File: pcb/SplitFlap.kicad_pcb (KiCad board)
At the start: 2 copper layers, 35 x 35 mm, 17 parts, among them U1 PCF8575DBR, U2 ULN2003

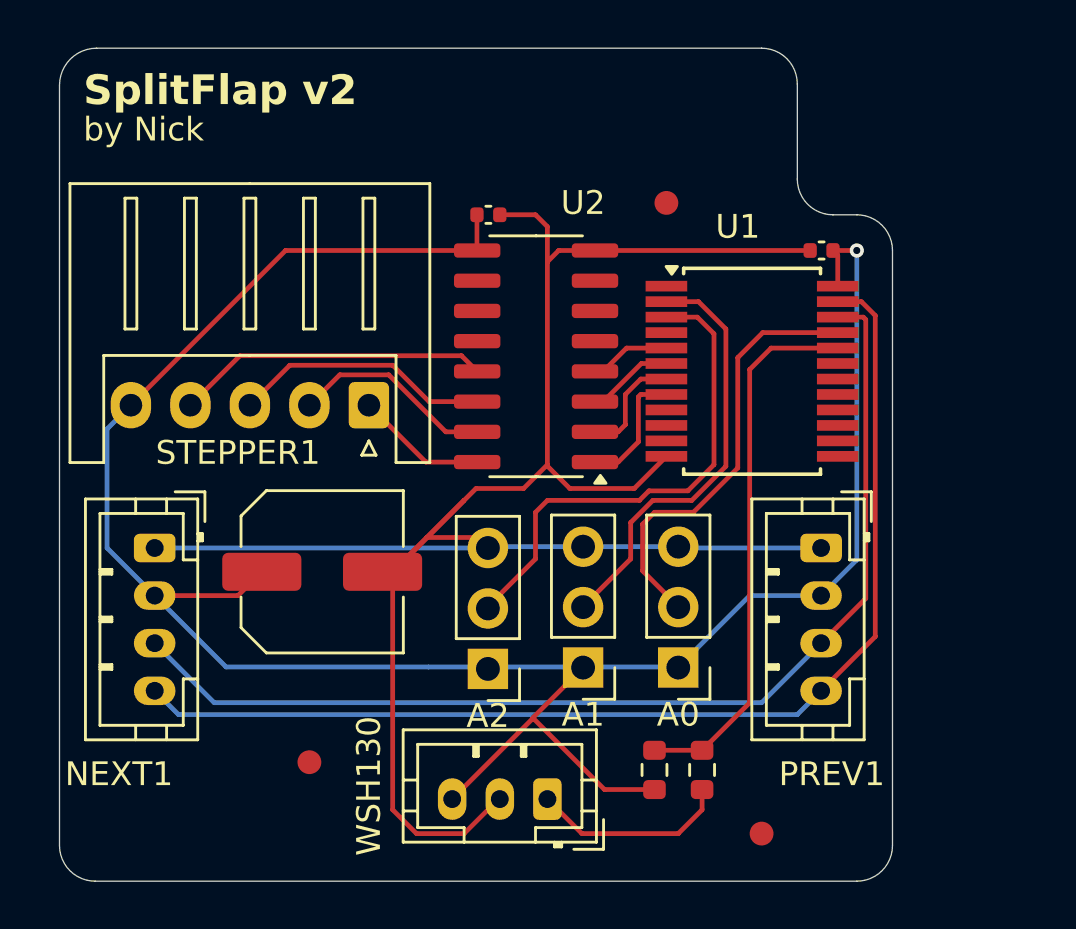
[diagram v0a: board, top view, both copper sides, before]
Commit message: Accomodate linear regulator and new address pins on PCB
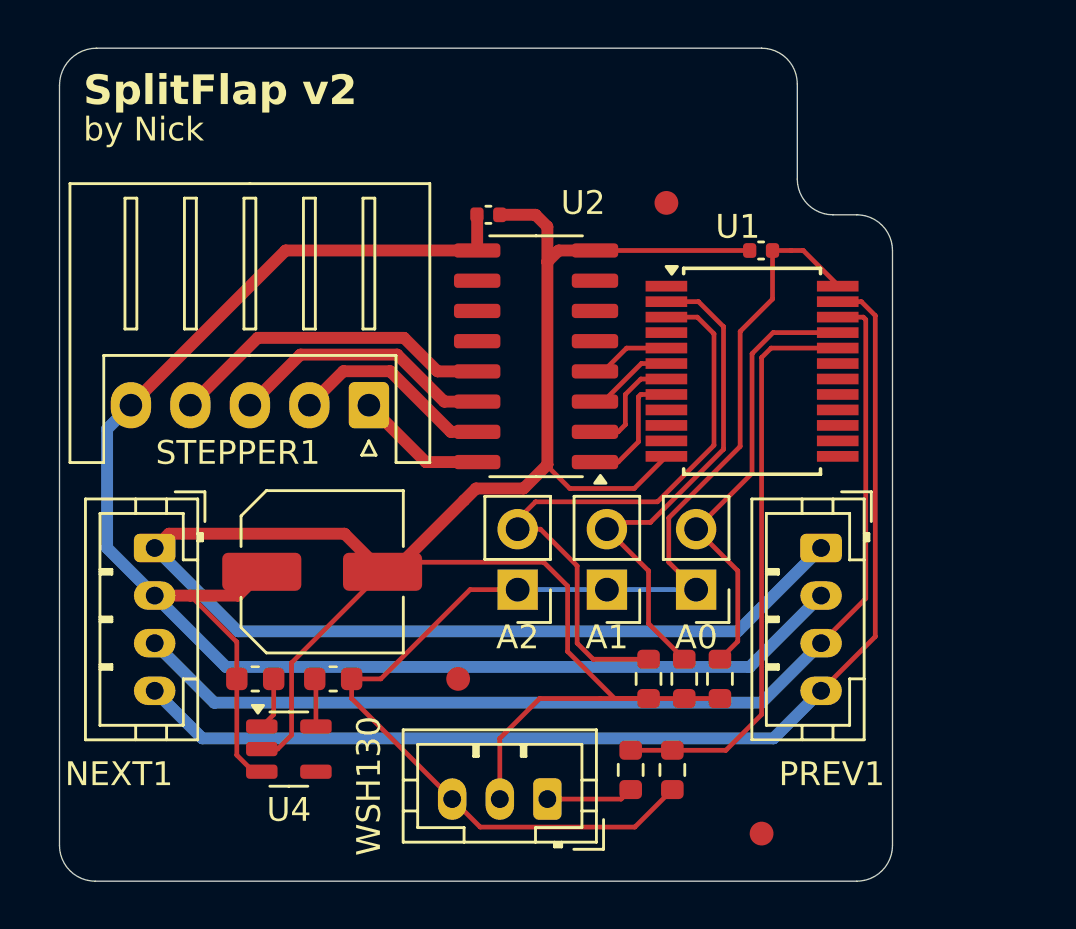
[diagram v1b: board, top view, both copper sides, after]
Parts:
- added C2: 1 µF, Capacitor_SMD:C_0603_1608Metric, F.Cu at (153.2, 86.0)
- added C3: 1 µF, Capacitor_SMD:C_0603_1608Metric, F.Cu at (156.5, 86.0)
- added PULL_UP3: 10K, Resistor_SMD:R_0603_1608Metric, F.Cu at (172.8, 86.0)
- added PULL_UP4: 10K, Resistor_SMD:R_0603_1608Metric, F.Cu at (171.2, 86.0)
- added PULL_UP5: 10K, Resistor_SMD:R_0603_1608Metric, F.Cu at (169.8, 86.0)
- added U4: AP2112K-3.3, Package_TO_SOT_SMD:SOT-23-5, F.Cu at (154.6, 89.0)
- A0, A1, A2: value Conn_01x03_Pin -> Conn_01x02_Pin; footprint Connector_PinHeader_2.54mm:PinHeader_1x03_P2.54mm_Vertical -> Connector_PinHeader_2.54mm:PinHeader_1x02_P2.54mm_Vertical
- moved REF** 7.16 mm to (161.8, 86.0)
- moved A2 3.56 mm to (164.2, 82.2)
- moved A1 3.42 mm to (168.0, 82.2)
- moved A0 3.36 mm to (171.8, 82.2)
- moved SERIES1 3.00 mm to (169.0, 89.8)
- moved C1 2.54 mm to (174.5, 68.0)
- moved PULL_UP2 0.75 mm to (170.8, 89.8)
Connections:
- A0 pad 1: +5V -> +3.3V
- A1 pad 1: +5V -> +3.3V
- A2 pad 1: +5V -> +3.3V
- C1 pad 1: +5V -> +3.3V
- C3_BULK1 pad 1: +5V -> GND
- C3_BULK1 pad 2: GND -> +5V
- PULL_UP2 pad 1: +5V -> +3.3V
- U1 pad 24: +5V -> +3.3V
- WSH130 pad 3: +5V -> +3.3V
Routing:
- net +3.3V: track 0.00 -> 53.5 mm
- net GND: track 89.5 -> 115.5 mm
- net +5V: track 95.5 -> 71.9 mm, vias 1 -> 0
- net Net-(A2-Pin_2): track 20.9 -> 26.2 mm
- net Net-(WSH130-Pin_1): track 8.36 -> 3.67 mm
- net Net-(A1-Pin_2): track 18.1 -> 20.7 mm
- net Net-(U4-VIN): track 0.00 -> 2.21 mm
- net Net-(U4-VOUT): track 0.00 -> 2.02 mm
- net Net-(U1-P17): track 22.9 -> 24.5 mm
- net Net-(NEXT1-Pin_4): track 47.4 -> 48.2 mm
- net Net-(STEPPER1-Pin_4): track 13.2 -> 13.8 mm

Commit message: Minor pcb changes
- Updates the position of the entire board down,
- Adds an edge cut section for the WSH130 wiring.
- Moves the ULN2003 up a bit to clean up the connections.
- Updates silkscreen labels.
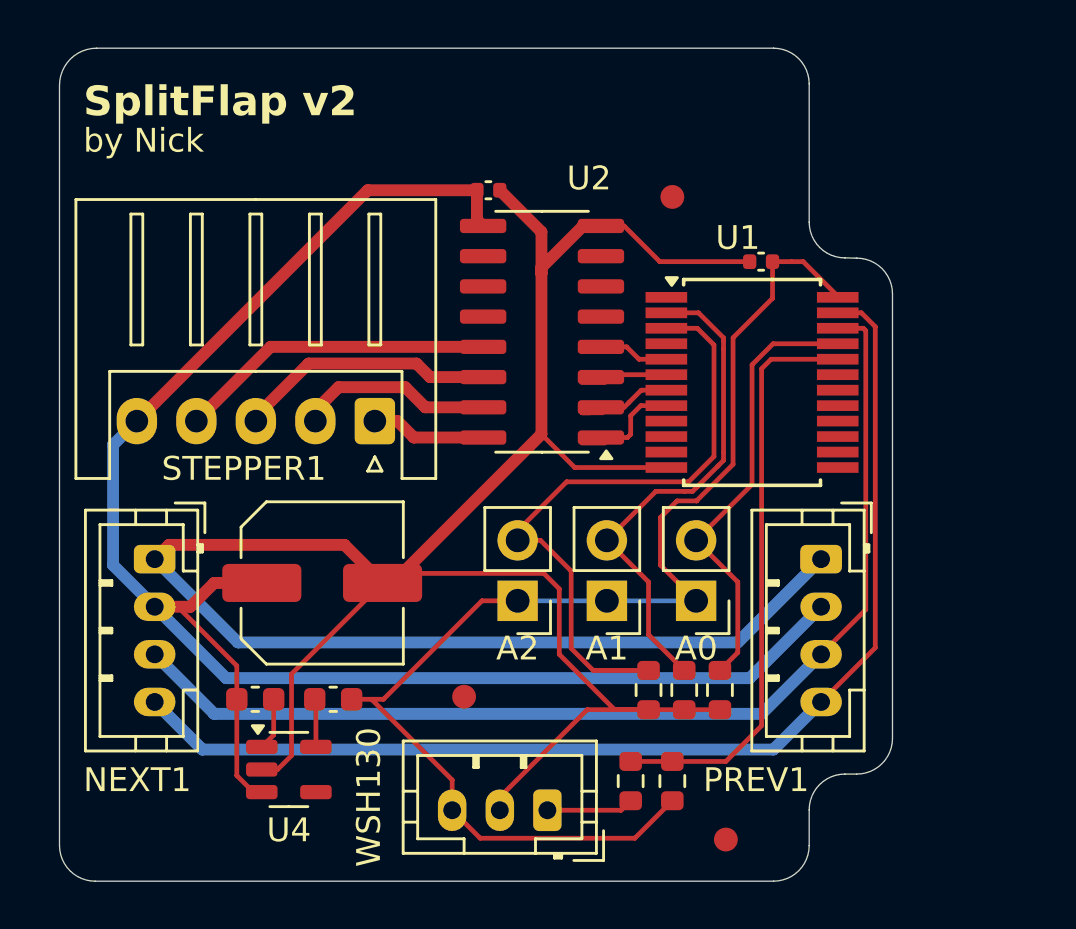
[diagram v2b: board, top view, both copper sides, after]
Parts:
- moved REF** 1.52 mm to (173.0, 92.8)
- moved U2 1.06 mm to (165.3, 71.4)
- moved C2_BYPASS1 1.03 mm to (163.0, 65.5)
- moved C2 0.86 mm to (153.2, 86.9)
- moved C3 0.86 mm to (156.5, 86.9)
- moved U4 0.86 mm to (154.6, 89.8)
- moved REF** 0.79 mm to (162.0, 86.8)
- moved STEPPER1 0.71 mm to (158.2, 75.2)
- moved WSH130 0.47 mm to (165.5, 91.5)
- moved A0 0.47 mm to (171.8, 82.7)
- moved A1 0.47 mm to (168.0, 82.7)
- moved A2 0.47 mm to (164.2, 82.7)
- moved C1 0.47 mm to (174.5, 68.5)
- moved C3_BULK1 0.47 mm to (156.0, 82.0)
- moved NEXT1 0.47 mm to (149.0, 81.0)
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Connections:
- C3_BULK1 pad 1: GND -> +5V
- C3_BULK1 pad 2: +5V -> GND
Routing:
- net +5V: track 71.9 -> 74.7 mm
- net Net-(U1-P4): track 6.44 -> 4.73 mm
- net Net-(U1-P1): track 4.38 -> 2.97 mm
- net Net-(U1-P3): track 5.64 -> 4.27 mm
- net Net-(U1-P2): track 4.88 -> 3.76 mm
- net Net-(STEPPER1-Pin_1): track 5.54 -> 4.84 mm
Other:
- outline, holes or cut-outs redrawn
- board text added: "+3.3V"

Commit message: Rewire PCB
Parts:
- removed A0, A1, A2: Conn_01x02_Pin, Connector_PinHeader_2.54mm:PinHeader_1x02_P2.54mm_Vertical
- added J1: A1_3, Connector_PinHeader_2.54mm:PinHeader_2x03_P2.54mm_Vertical, F.Cu at (177.0, 74.0)
- added PULL_UP6: 4K7, Resistor_SMD:R_0603_1608Metric, F.Cu at (162.8, 85.5)
- added PULL_UP7: 4k7, Resistor_SMD:R_0603_1608Metric, F.Cu at (162.8, 84.0)
- added PULL_UP8: 4k7, Resistor_SMD:R_0603_1608Metric, F.Cu at (162.8, 82.5)
- added PULL_UP9: 4k7, Resistor_SMD:R_0603_1608Metric, F.Cu at (162.8, 81.0)
- moved REF** 23.3 mm to (149.8, 91.8)
- moved C1 20.2 mm to (172.2, 88.5)
- moved PULL_UP5 17.9 mm to (174.0, 69.1), turned to 90 degrees
- moved PULL_UP3 17.5 mm to (171.0, 69.1), turned to 90 degrees
- moved PULL_UP4 17.4 mm to (172.5, 69.1), turned to 90 degrees
- moved REF** 13.1 mm to (174.0, 92.0)
- moved U1 10.8 mm to (169.1, 83.1), turned to -90 degrees
- moved REF** 4.78 mm to (174.0, 62.2)
- moved PULL_UP2 1.60 mm to (169.2, 89.8)
- moved C2_BYPASS1 1.55 mm to (162.4, 66.9)
- moved SERIES1 1.36 mm to (167.8, 89.8)
- moved WSH130 1.27 mm to (164.2, 91.3)
- moved U2 1.24 mm to (165.2, 72.7)
- moved C3 0.60 mm to (155.9, 87.1)
- moved C2 0.33 mm to (153.0, 87.1), turned to 180 degrees
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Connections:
- C2 pad 1: +5V -> GND
- C2 pad 2: Net-(U4-VIN) -> +5V
- C3 pad 1: Net-(U4-VOUT) -> GND
- PULL_UP3 pad 1: Net-(A0-Pin_2) -> Net-(J1-Pin_6)
- PULL_UP5 pad 1: Net-(A2-Pin_2) -> Net-(J1-Pin_2)
- U1 pad 21: Net-(A0-Pin_2) -> Net-(J1-Pin_2)
- U1 pad 3: Net-(A2-Pin_2) -> Net-(J1-Pin_6)
- U4 pad 1: Net-(U4-VIN) -> +5V
- U4 pad 5: Net-(U4-VOUT) -> +3.3V
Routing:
- net Net-(A2-Pin_2): track 26.2 -> 0.00 mm
- net Net-(J1-Pin_2): track 0.00 -> 21.0 mm
- net Net-(U1-P17): track 24.5 -> 4.06 mm
- net Net-(A0-Pin_2): track 18.5 -> 0.00 mm
- net Net-(U1-P1): track 2.97 -> 17.3 mm
- net Net-(NEXT1-Pin_4): track 48.2 -> 34.7 mm
- net Net-(U1-P2): track 3.76 -> 15.5 mm
- net Net-(NEXT1-Pin_3): track 45.7 -> 35.0 mm
- net Net-(J1-Pin_6): track 0.00 -> 10.4 mm
- net Net-(J1-Pin_4): track 20.7 -> 11.8 mm
- net Net-(U1-P3): track 4.27 -> 13.2 mm
- net +3.3V: track 53.7 -> 62.5 mm
- net GND: track 116.0 -> 120.6 mm
- net Net-(U1-P4): track 4.73 -> 9.33 mm
- net +5V: track 74.7 -> 71.5 mm
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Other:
- board text added: "A1"
- board text added: "A2"
- board text added: "A3"
- board text added: "SplitFlap v3"
- board text removed: "SplitFlap v2"

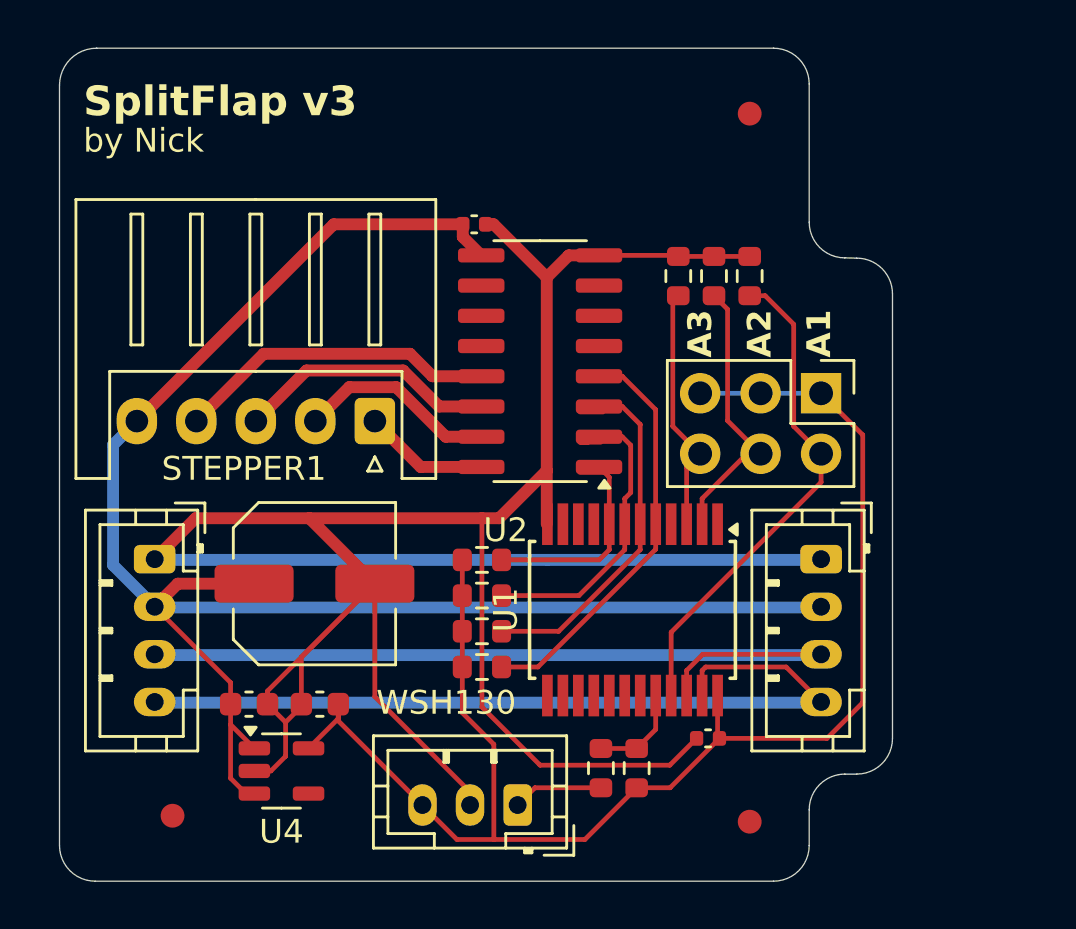
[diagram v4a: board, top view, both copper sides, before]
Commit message: Eliminate 3.3v line from PCB
Based on the findings by FoxManJ the 3.3v line is not required if we
use a 4.7k Ohm pull-up to 5v for the SCL and SDA lines coming from the
ESP32.

By using this pull-up to 5V we eliminate the need for the PCF8575 to
run at 3.3v to understand the signals from the ESP32, which was the
reason I originally implemented the 3.3v line on each board.
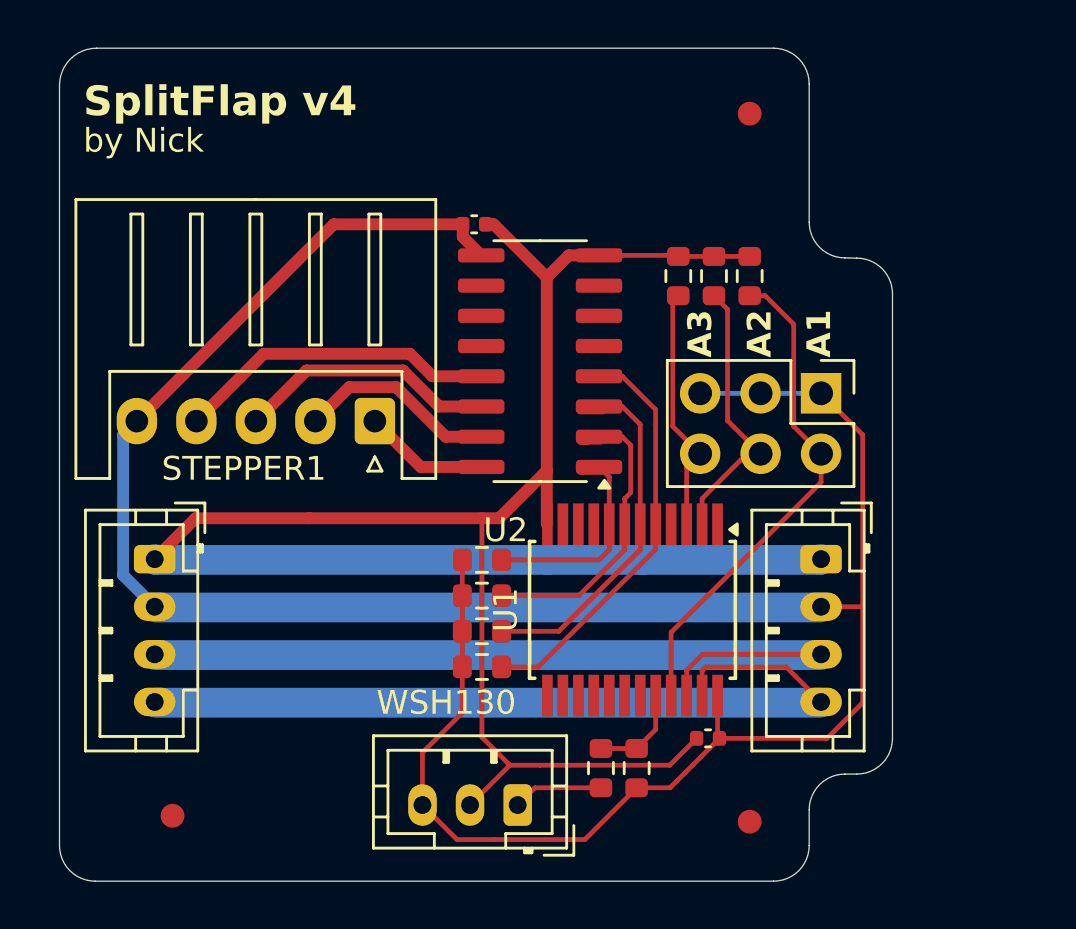
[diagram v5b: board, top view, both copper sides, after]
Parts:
- removed C2, C3: 1 µF, Capacitor_SMD:C_0603_1608Metric
- removed C3_BULK1: 220 µF, Capacitor_SMD:C_Elec_6.3x7.7
- removed U4: AP2112K-3.3, Package_TO_SOT_SMD:SOT-23-5
- PULL_DOWN3: renamed from PULL_UP3; value 10K -> 47K
- PULL_DOWN4: renamed from PULL_UP4; value 10K -> 47K
- PULL_DOWN5: renamed from PULL_UP5; value 10K -> 47K
- PULL_UP6: value 4K7 -> 2k2
- PULL_UP7, PULL_UP8, PULL_UP9: value 4k7 -> 2k2
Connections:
- C1 pad 1: +3.3V -> +5V
- J1 pad 1: +3.3V -> +5V
- J1 pad 3: +3.3V -> +5V
- J1 pad 5: +3.3V -> +5V
- PULL_UP2 pad 1: +3.3V -> +5V
- PULL_UP6 pad 1: +3.3V -> +5V
- PULL_UP7 pad 1: +3.3V -> +5V
- PULL_UP8 pad 1: +3.3V -> +5V
- PULL_UP9 pad 1: +3.3V -> +5V
- U1 pad 24: +3.3V -> +5V
- WSH130 pad 3: +3.3V -> +5V
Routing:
- net +3.3V: track 62.5 -> 0.00 mm
- net +5V: track 71.5 -> 110.2 mm
- net GND: track 120.6 -> 91.0 mm
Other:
- board text added: "SplitFlap v4"
- board text removed: "SplitFlap v3"

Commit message: Use pinsocket and headers for board to board connector
Eliminates the JST cables between boards.
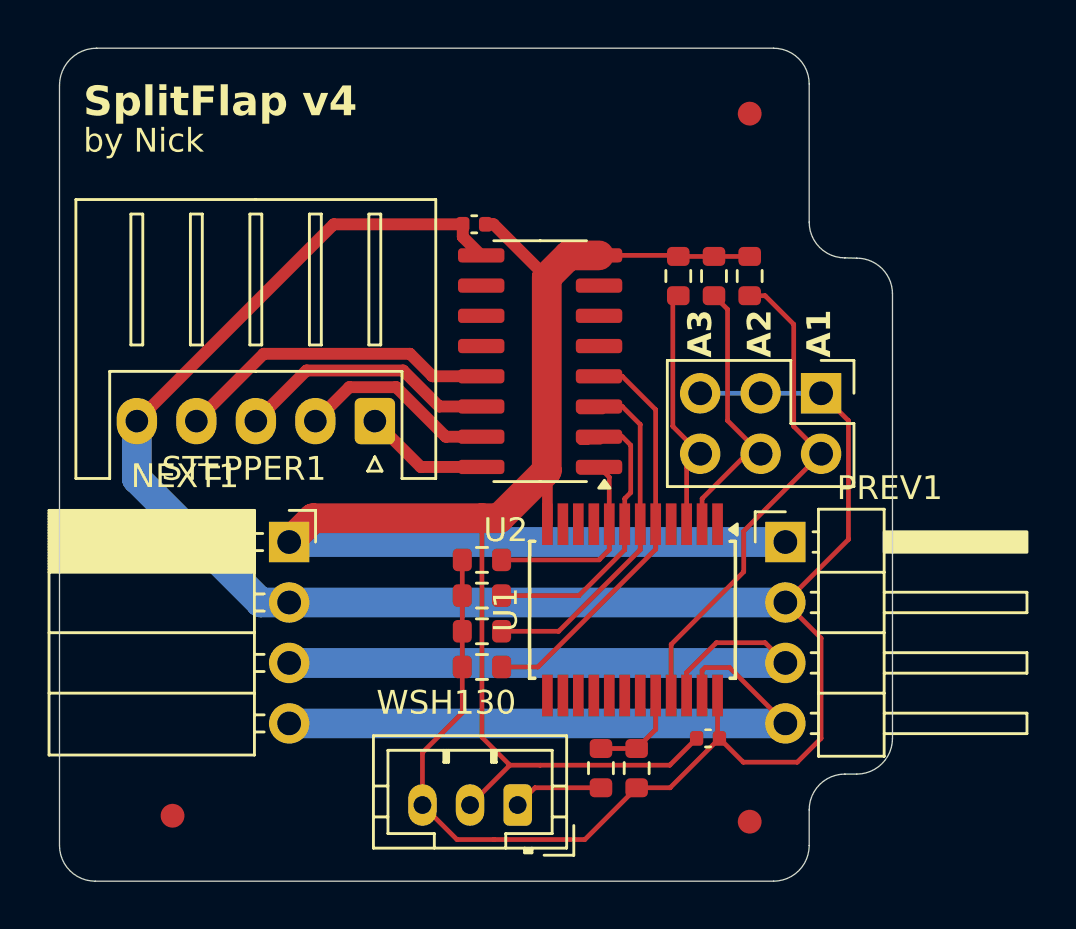
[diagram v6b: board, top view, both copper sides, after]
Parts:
- NEXT1: footprint Connector_JST:JST_PH_B4B-PH-K_1x04_P2.00mm_Vertical -> Connector_PinSocket_2.54mm:PinSocket_1x04_P2.54mm_Horizontal
- PREV1: footprint Connector_JST:JST_PH_B4B-PH-K_1x04_P2.00mm_Vertical -> Connector_PinHeader_2.54mm:PinHeader_1x04_P2.54mm_Horizontal
- moved NEXT1 5.70 mm to (154.7, 80.2), turned to 0 degrees
- moved PREV1 1.66 mm to (175.5, 80.2), turned to 0 degrees
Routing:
- net GND: track 91.0 -> 77.8 mm
- net Net-(NEXT1-Pin_4): track 34.7 -> 26.4 mm
- net Net-(NEXT1-Pin_3): track 35.0 -> 26.8 mm
- net +5V: track 110.2 -> 105.1 mm
